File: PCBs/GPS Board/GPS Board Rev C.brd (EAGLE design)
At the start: 95.9 x 90.2 mm, 11 parts

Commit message: Update piNAV connector to PE-BE model
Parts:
- PINAV-CONNECTOR: value HLE-110-02-X-DV-BE-A -> HLE-110-02-X-DVHLE-110-X-DV-PE-BA; device HLE-110-02-X-DV-BE-A:HLE-110-02-X-DV-BE-A -> HLE-110-02-X-DV:HLE-110-02-X-DV-PE-BE
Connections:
- net GND: now also PINAV-CONNECTOR.P$15, PINAV-CONNECTOR.P$7; no longer PINAV-CONNECTOR.15, PINAV-CONNECTOR.7
- net PF: now also PINAV-CONNECTOR.P$6; no longer PINAV-CONNECTOR.6
- net RX: now also PINAV-CONNECTOR.P$2; no longer PINAV-CONNECTOR.2
- net SW9: now also PINAV-CONNECTOR.P$14, PINAV-CONNECTOR.P$8; no longer PINAV-CONNECTOR.14, PINAV-CONNECTOR.8
- net TX: now also PINAV-CONNECTOR.P$1; no longer PINAV-CONNECTOR.1
- net VPP: now also PINAV-CONNECTOR.P$5; no longer PINAV-CONNECTOR.5
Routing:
- net GND: track 12.5 -> 5.72 mm, vias 5 -> 3
- net SW9: track 134.0 -> 132.0 mm
- net TX: track 93.1 -> 92.2 mm
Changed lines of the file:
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@@
 <attribute name="TP_SIGNAL_NAME" value="" x="16.51" y="58.42" size="1.778" layer="27" display="off"/>
 </element>
-<element name="PINAV-CONNECTOR" library="HLE-110-02-X-DV-BE-A" package="HLE-110-02-X-DV-BE-A" value="HLE-110-02-X-DV-BE-A" x="44.069" y="72.39"/>
+<element name="PINAV-CONNECTOR" library="HLE-110-02-X-DV" package="HLE-110-02-X-DV-PE-BE" value="HLE-110-02-X-DVHLE-110-X-DV-PE-BA" x="44.069" y="72.39" smashed="yes">
+<attribute name="NAME" x="31.369" y="77.089" size="1.27" layer="25"/>
+</element>
 <element name="PINAV" library="Cubesat" package="PINAV-L1" value="" x="26.035" y="8.89"/>
 </elements>
@@
 <contactref element="U$2" pad="71"/>
 <wire x1="88.265" y1="53.34" x2="86.995" y2="54.61" width="0.2032" layer="1"/>
-<contactref element="PINAV-CONNECTOR" pad="14"/>
+<contactref element="PINAV-CONNECTOR" pad="P$14"/>
 <contactref element="C1" pad="1"/>
 <contactref element="C2" pad="1"/>
-<contactref element="PINAV-CONNECTOR" pad="8"/>
+<contactref element="PINAV-CONNECTOR" pad="P$8"/>
 <contactref element="3V3" pad="TP"/>
 <wire x1="66.548" y1="84.77" x2="64.135" y2="84.77" width="0.508" layer="1"/>
 <wire x1="64.135" y1="84.77" x2="44.45" y2="84.77" width="0.508" layer="1"/>
 <wire x1="44.45" y1="84.77" x2="44.257" y2="84.77" width="0.508" layer="1"/>
-<wire x1="40.259" y1="80.772" x2="40.259" y2="75.2348" width="0.508" layer="1"/>
+<wire x1="40.259" y1="80.772" x2="40.259" y2="76.2" width="0.508" layer="1"/>
 <wire x1="44.257" y1="84.77" x2="40.259" y2="80.772" width="0.508" layer="1"/>
 <wire x1="44.45" y1="84.77" x2="47.879" y2="81.341" width="0.508" layer="1"/>
-<wire x1="47.879" y1="81.341" x2="47.879" y2="75.2348" width="0.508" layer="1"/>
+<wire x1="47.879" y1="81.341" x2="47.879" y2="76.2" width="0.508" layer="1"/>
 <wire x1="44.45" y1="84.77" x2="23.81" y2="84.77" width="0.2032" layer="1"/>
 <wire x1="23.81" y1="84.77" x2="16.51" y2="77.47" width="0.2032" layer="1"/>
@@
 <contactref element="U$2" pad="84"/>
 <contactref element="U$2" pad="100"/>
-<contactref element="PINAV-CONNECTOR" pad="7"/>
-<contactref element="PINAV-CONNECTOR" pad="15"/>
+<contactref element="PINAV-CONNECTOR" pad="P$7"/>
+<contactref element="PINAV-CONNECTOR" pad="P$15"/>
 <contactref element="C1" pad="2"/>
 <contactref element="C2" pad="2"/>
@@
 <contactref element="U$2" pad="99"/>
 <contactref element="GND" pad="TP"/>
-<wire x1="47.879" y1="69.5452" x2="47.879" y2="66.167" width="0.2032" layer="1"/>
-<via x="47.879" y="66.167" extent="1-16" drill="0.254"/>
-<wire x1="37.719" y1="69.5452" x2="37.719" y2="66.167" width="0.2032" layer="1"/>
-<via x="37.719" y="66.167" extent="1-16" drill="0.254"/>
 <wire x1="16.51" y1="43.18" x2="19.05" y2="43.18" width="0.2032" layer="1"/>
 <via x="19.05" y="43.18" extent="1-16" drill="0.254"/>
@@
 <contactref element="U$2" pad="23"/>
 <wire x1="83.185" y1="48.26" x2="60.96" y2="70.485" width="0.2032" layer="1"/>
-<contactref element="PINAV-CONNECTOR" pad="5"/>
+<contactref element="PINAV-CONNECTOR" pad="P$5"/>
 <contactref element="VPP" pad="TP"/>
 <wire x1="54.61" y1="81.28" x2="51.689" y2="78.359" width="0.2032" layer="1"/>
-<wire x1="51.689" y1="78.359" x2="51.689" y2="70.739" width="0.2032" layer="1"/>
-<wire x1="51.689" y1="70.739" x2="50.4952" y2="69.5452" width="0.2032" layer="1"/>
-<wire x1="50.4952" y1="69.5452" x2="50.419" y2="69.5452" width="0.2032" layer="1"/>
-<wire x1="50.419" y1="69.5452" x2="50.419" y2="65.024" width="0.2032" layer="1"/>
+<wire x1="50.419" y1="68.58" x2="50.419" y2="65.024" width="0.2032" layer="1"/>
 <wire x1="40.005" y1="54.61" x2="16.51" y2="54.61" width="0.2032" layer="1"/>
 <wire x1="50.419" y1="65.024" x2="40.005" y2="54.61" width="0.2032" layer="1"/>
+<wire x1="51.689" y1="69.85" x2="50.419" y2="68.58" width="0.2032" layer="1"/>
+<wire x1="51.689" y1="78.359" x2="51.689" y2="69.85" width="0.2032" layer="1"/>
 </signal>
 <signal name="PF">
@@
 <contactref element="U$2" pad="24"/>
 <wire x1="85.725" y1="48.26" x2="84.455" y2="49.53" width="0.2032" layer="1"/>
-<contactref element="PINAV-CONNECTOR" pad="6"/>
+<contactref element="PINAV-CONNECTOR" pad="P$6"/>
 <contactref element="PF" pad="TP"/>
 <wire x1="54.102" y1="82.042" x2="50.419" y2="78.359" width="0.2032" layer="1"/>
-<wire x1="50.419" y1="78.359" x2="50.419" y2="75.2348" width="0.2032" layer="1"/>
-<wire x1="50.419" y1="75.2348" x2="49.9618" y2="75.2348" width="0.2032" layer="1"/>
-<wire x1="49.9618" y1="75.2348" x2="49.149" y2="74.422" width="0.2032" layer="1"/>
-<wire x1="49.149" y1="74.422" x2="49.149" y2="65.659" width="0.2032" layer="1"/>
+<wire x1="50.419" y1="78.359" x2="50.419" y2="76.2" width="0.2032" layer="1"/>
 <wire x1="41.91" y1="58.42" x2="16.51" y2="58.42" width="0.2032" layer="1"/>
 <wire x1="49.149" y1="65.659" x2="41.91" y2="58.42" width="0.2032" layer="1"/>
+<wire x1="50.419" y1="76.2" x2="49.149" y2="74.93" width="0.2032" layer="1"/>
+<wire x1="49.149" y1="74.93" x2="49.149" y2="65.659" width="0.2032" layer="1"/>
 </signal>
 <signal name="TX">
 <contactref element="U$2" pad="33"/>
-<contactref element="PINAV-CONNECTOR" pad="1"/>
+<contactref element="PINAV-CONNECTOR" pad="P$1"/>
 <contactref element="TX" pad="TP"/>
-<wire x1="55.499" y1="69.5452" x2="58.42" y2="66.6242" width="0.2032" layer="1"/>
-<wire x1="58.42" y1="66.6242" x2="58.42" y2="60.96" width="0.2032" layer="1"/>
 <wire x1="58.42" y1="60.96" x2="83.185" y2="36.195" width="0.2032" layer="1"/>
 <wire x1="83.185" y1="36.195" x2="83.185" y2="35.56" width="0.2032" layer="1"/>
 <wire x1="58.42" y1="60.96" x2="44.45" y2="46.99" width="0.2032" layer="1"/>
 <wire x1="44.45" y1="46.99" x2="16.51" y2="46.99" width="0.2032" layer="1"/>
+<wire x1="55.499" y1="68.58" x2="58.42" y2="65.659" width="0.2032" layer="1"/>
+<wire x1="58.42" y1="65.659" x2="58.42" y2="60.96" width="0.2032" layer="1"/>
 </signal>
 <signal name="RX">
@@
 <wire x1="84.455" y1="34.29" x2="83.185" y2="33.02" width="0.2032" layer="1"/>
 <wire x1="81.915" y1="39.37" x2="83.82" y2="39.37" width="0.2032" layer="1"/>
-<contactref element="PINAV-CONNECTOR" pad="2"/>
+<contactref element="PINAV-CONNECTOR" pad="P$2"/>
 <contactref element="RX" pad="TP"/>
-<wire x1="55.499" y1="75.2348" x2="56.8452" y2="75.2348" width="0.2032" layer="1"/>
 <wire x1="59.69" y1="61.595" x2="81.915" y2="39.37" width="0.2032" layer="1"/>
-<wire x1="56.8452" y1="75.2348" x2="59.69" y2="72.39" width="0.2032" layer="1"/>
 <wire x1="59.69" y1="72.39" x2="59.69" y2="61.595" width="0.2032" layer="1"/>
 <wire x1="83.185" y1="33.02" x2="21.59" y2="33.02" width="0.2032" layer="1"/>
@@
 <wire x1="12.7" y1="41.91" x2="12.7" y2="46.99" width="0.2032" layer="1"/>
 <wire x1="12.7" y1="46.99" x2="16.51" y2="50.8" width="0.2032" layer="1"/>
+<wire x1="55.499" y1="76.2" x2="55.88" y2="76.2" width="0.2032" layer="1"/>
+<wire x1="55.88" y1="76.2" x2="59.69" y2="72.39" width="0.2032" layer="1"/>
 </signal>
 </signals>

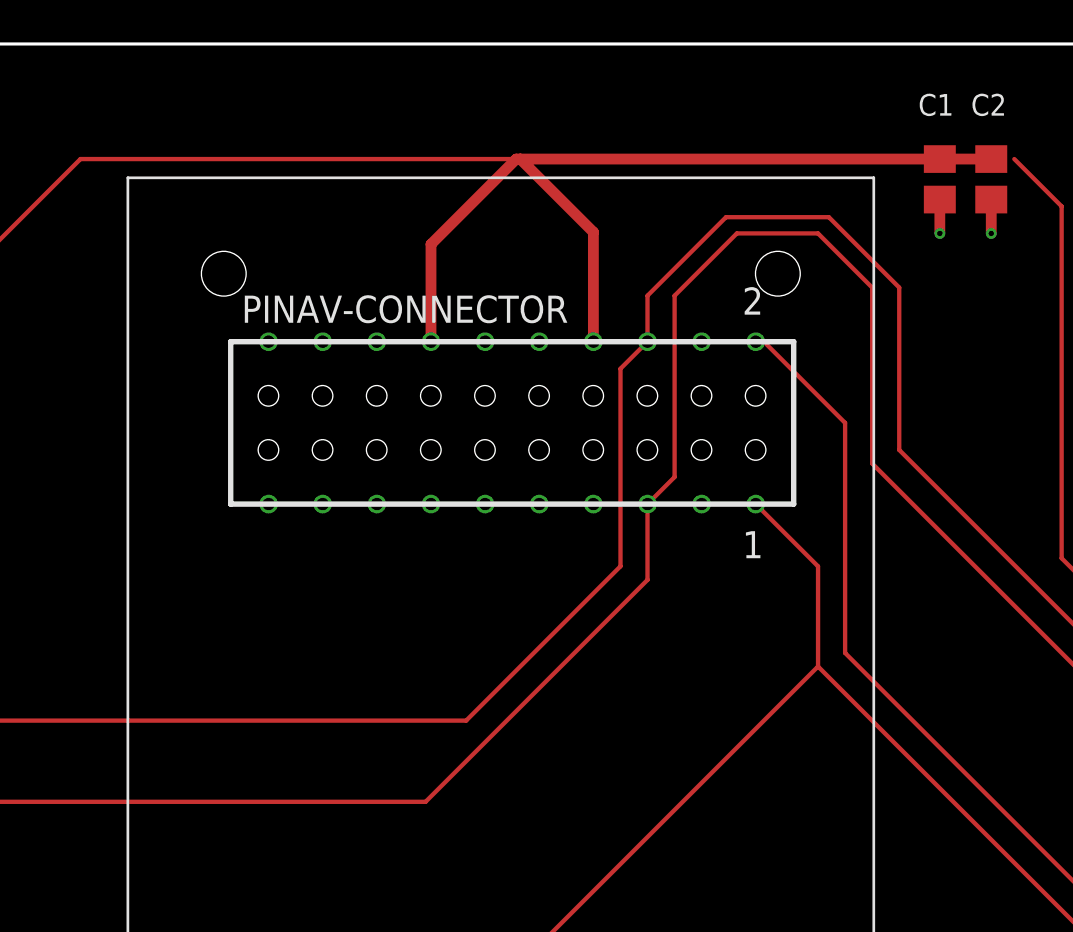
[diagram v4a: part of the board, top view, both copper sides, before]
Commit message: Update bus definition
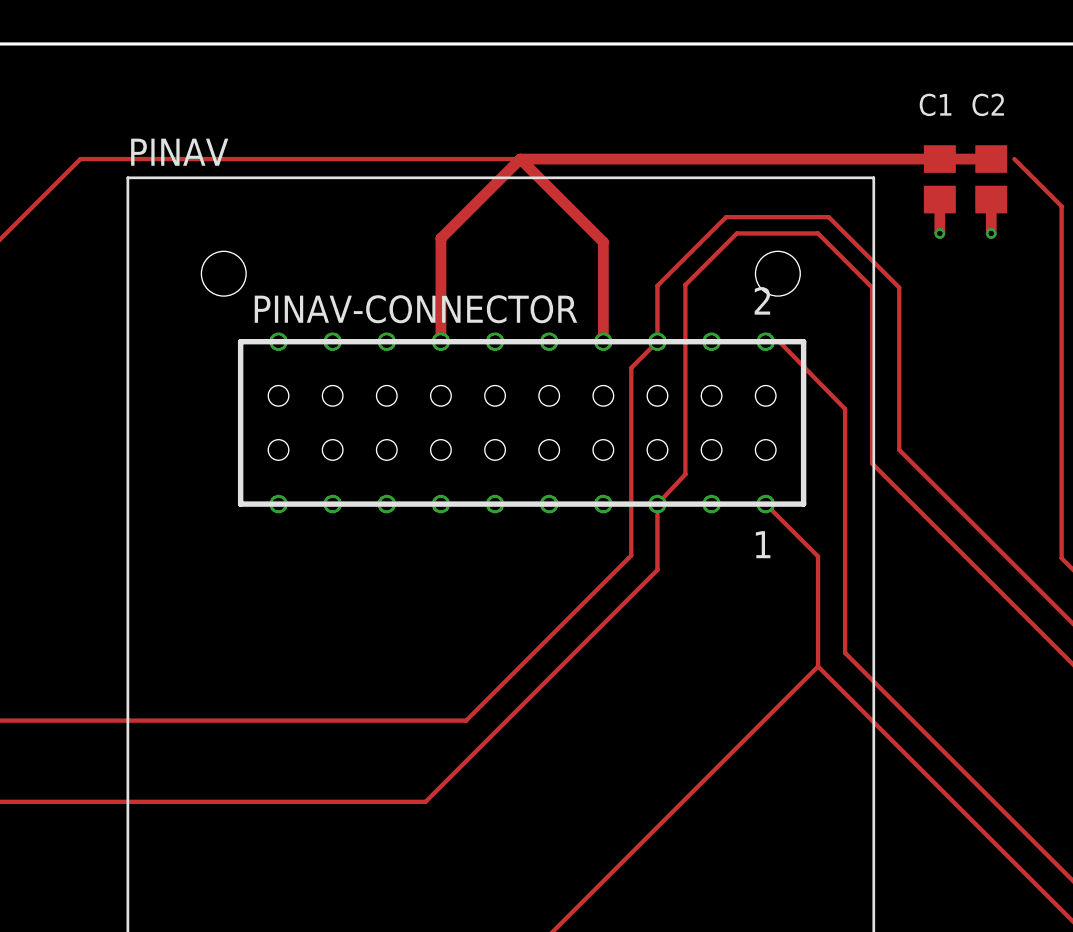
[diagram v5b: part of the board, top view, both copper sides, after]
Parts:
- moved PINAV-CONNECTOR 0.47 mm to (44.5, 72.4)
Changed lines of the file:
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@@
 <attribute name="TP_SIGNAL_NAME" value="" x="16.51" y="58.42" size="1.778" layer="27" display="off"/>
 </element>
-<element name="PINAV-CONNECTOR" library="HLE-110-02-X-DV" package="HLE-110-02-X-DV-PE-BE" value="HLE-110-02-X-DVHLE-110-X-DV-PE-BA" x="44.069" y="72.39" smashed="yes">
-<attribute name="NAME" x="31.369" y="77.089" size="1.27" layer="25"/>
+<element name="PINAV-CONNECTOR" library="HLE-110-02-X-DV" package="HLE-110-02-X-DV-PE-BE" value="HLE-110-02-X-DVHLE-110-X-DV-PE-BA" x="44.535" y="72.39" smashed="yes">
+<attribute name="NAME" x="31.835" y="77.089" size="1.27" layer="25"/>
 </element>
 <element name="PINAV" library="Cubesat" package="PINAV-L1" value="" x="26.035" y="8.89"/>
@@
 <contactref element="3V3" pad="TP"/>
 <wire x1="66.548" y1="84.77" x2="64.135" y2="84.77" width="0.508" layer="1"/>
-<wire x1="64.135" y1="84.77" x2="44.45" y2="84.77" width="0.508" layer="1"/>
-<wire x1="44.45" y1="84.77" x2="44.257" y2="84.77" width="0.508" layer="1"/>
-<wire x1="40.259" y1="80.772" x2="40.259" y2="76.2" width="0.508" layer="1"/>
-<wire x1="44.257" y1="84.77" x2="40.259" y2="80.772" width="0.508" layer="1"/>
-<wire x1="44.45" y1="84.77" x2="47.879" y2="81.341" width="0.508" layer="1"/>
-<wire x1="47.879" y1="81.341" x2="47.879" y2="76.2" width="0.508" layer="1"/>
+<wire x1="64.135" y1="84.77" x2="44.535" y2="84.77" width="0.508" layer="1"/>
+<wire x1="44.535" y1="84.77" x2="44.45" y2="84.77" width="0.2032" layer="1"/>
 <wire x1="44.45" y1="84.77" x2="23.81" y2="84.77" width="0.2032" layer="1"/>
 <wire x1="23.81" y1="84.77" x2="16.51" y2="77.47" width="0.2032" layer="1"/>
 <wire x1="16.51" y1="77.47" x2="16.51" y2="62.23" width="0.2032" layer="1"/>
+<wire x1="40.725" y1="76.2" x2="40.725" y2="81.045" width="0.508" layer="1"/>
+<wire x1="40.725" y1="81.045" x2="44.45" y2="84.77" width="0.508" layer="1"/>
+<wire x1="48.345" y1="76.2" x2="48.345" y2="80.875" width="0.508" layer="1"/>
+<wire x1="48.345" y1="80.875" x2="44.45" y2="84.77" width="0.508" layer="1"/>
 <wire x1="66.548" y1="84.77" x2="67.63" y2="84.77" width="0" layer="19" extent="1-1"/>
 </signal>
@@
 <contactref element="PINAV-CONNECTOR" pad="P$5"/>
 <contactref element="VPP" pad="TP"/>
-<wire x1="54.61" y1="81.28" x2="51.689" y2="78.359" width="0.2032" layer="1"/>
-<wire x1="50.419" y1="68.58" x2="50.419" y2="65.024" width="0.2032" layer="1"/>
+<wire x1="54.61" y1="81.28" x2="52.197" y2="78.867" width="0.2032" layer="1"/>
 <wire x1="40.005" y1="54.61" x2="16.51" y2="54.61" width="0.2032" layer="1"/>
-<wire x1="50.419" y1="65.024" x2="40.005" y2="54.61" width="0.2032" layer="1"/>
-<wire x1="51.689" y1="69.85" x2="50.419" y2="68.58" width="0.2032" layer="1"/>
-<wire x1="51.689" y1="78.359" x2="51.689" y2="69.85" width="0.2032" layer="1"/>
+<wire x1="52.197" y1="69.977" x2="50.885" y2="68.58" width="0.2032" layer="1"/>
+<wire x1="52.197" y1="78.867" x2="52.197" y2="69.977" width="0.2032" layer="1"/>
+<wire x1="50.885" y1="68.58" x2="50.885" y2="65.49" width="0.2032" layer="1"/>
+<wire x1="50.885" y1="65.49" x2="40.005" y2="54.61" width="0.2032" layer="1"/>
 </signal>
 <signal name="PF">
@@
 <contactref element="PINAV-CONNECTOR" pad="P$6"/>
 <contactref element="PF" pad="TP"/>
-<wire x1="54.102" y1="82.042" x2="50.419" y2="78.359" width="0.2032" layer="1"/>
-<wire x1="50.419" y1="78.359" x2="50.419" y2="76.2" width="0.2032" layer="1"/>
 <wire x1="41.91" y1="58.42" x2="16.51" y2="58.42" width="0.2032" layer="1"/>
-<wire x1="49.149" y1="65.659" x2="41.91" y2="58.42" width="0.2032" layer="1"/>
-<wire x1="50.419" y1="76.2" x2="49.149" y2="74.93" width="0.2032" layer="1"/>
-<wire x1="49.149" y1="74.93" x2="49.149" y2="65.659" width="0.2032" layer="1"/>
+<wire x1="49.657" y1="66.167" x2="49.53" y2="66.04" width="0.2032" layer="1"/>
+<wire x1="49.53" y1="66.04" x2="41.91" y2="58.42" width="0.2032" layer="1"/>
+<wire x1="54.102" y1="82.042" x2="54.102" y2="82.042" width="0.2032" layer="1"/>
+<wire x1="54.102" y1="82.042" x2="50.885" y2="78.825" width="0.2032" layer="1"/>
+<wire x1="50.885" y1="78.825" x2="50.885" y2="76.2" width="0.2032" layer="1"/>
+<wire x1="50.885" y1="76.2" x2="49.657" y2="74.972" width="0.2032" layer="1"/>
+<wire x1="49.657" y1="74.972" x2="49.657" y2="66.167" width="0.2032" layer="1"/>
 </signal>
 <signal name="TX">
@@
 <wire x1="58.42" y1="60.96" x2="44.45" y2="46.99" width="0.2032" layer="1"/>
 <wire x1="44.45" y1="46.99" x2="16.51" y2="46.99" width="0.2032" layer="1"/>
-<wire x1="55.499" y1="68.58" x2="58.42" y2="65.659" width="0.2032" layer="1"/>
-<wire x1="58.42" y1="65.659" x2="58.42" y2="60.96" width="0.2032" layer="1"/>
+<wire x1="55.965" y1="68.58" x2="58.42" y2="66.125" width="0.2032" layer="1"/>
+<wire x1="58.42" y1="66.125" x2="58.42" y2="60.96" width="0.2032" layer="1"/>
 </signal>
 <signal name="RX">
@@
 <contactref element="RX" pad="TP"/>
 <wire x1="59.69" y1="61.595" x2="81.915" y2="39.37" width="0.2032" layer="1"/>
-<wire x1="59.69" y1="72.39" x2="59.69" y2="61.595" width="0.2032" layer="1"/>
+<wire x1="59.69" y1="73.039490625" x2="59.69" y2="61.595" width="0.2032" layer="1"/>
 <wire x1="83.185" y1="33.02" x2="21.59" y2="33.02" width="0.2032" layer="1"/>
 <wire x1="21.59" y1="33.02" x2="12.7" y2="41.91" width="0.2032" layer="1"/>
 <wire x1="12.7" y1="41.91" x2="12.7" y2="46.99" width="0.2032" layer="1"/>
 <wire x1="12.7" y1="46.99" x2="16.51" y2="50.8" width="0.2032" layer="1"/>
-<wire x1="55.499" y1="76.2" x2="55.88" y2="76.2" width="0.2032" layer="1"/>
-<wire x1="55.88" y1="76.2" x2="59.69" y2="72.39" width="0.2032" layer="1"/>
+<wire x1="56.6" y1="76.2" x2="59.69" y2="73.039490625" width="0.2032" layer="1"/>
+<wire x1="55.965" y1="76.2" x2="56.6" y2="76.2" width="0.2032" layer="1"/>
 </signal>
 </signals>
